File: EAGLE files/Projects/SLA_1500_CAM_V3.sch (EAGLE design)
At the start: 90 parts, among them J4 MOLEX 53398-0471, J5 MOLEX 53398-04, U11 TXS0102, U8 TXS0102, U9 TXS0102

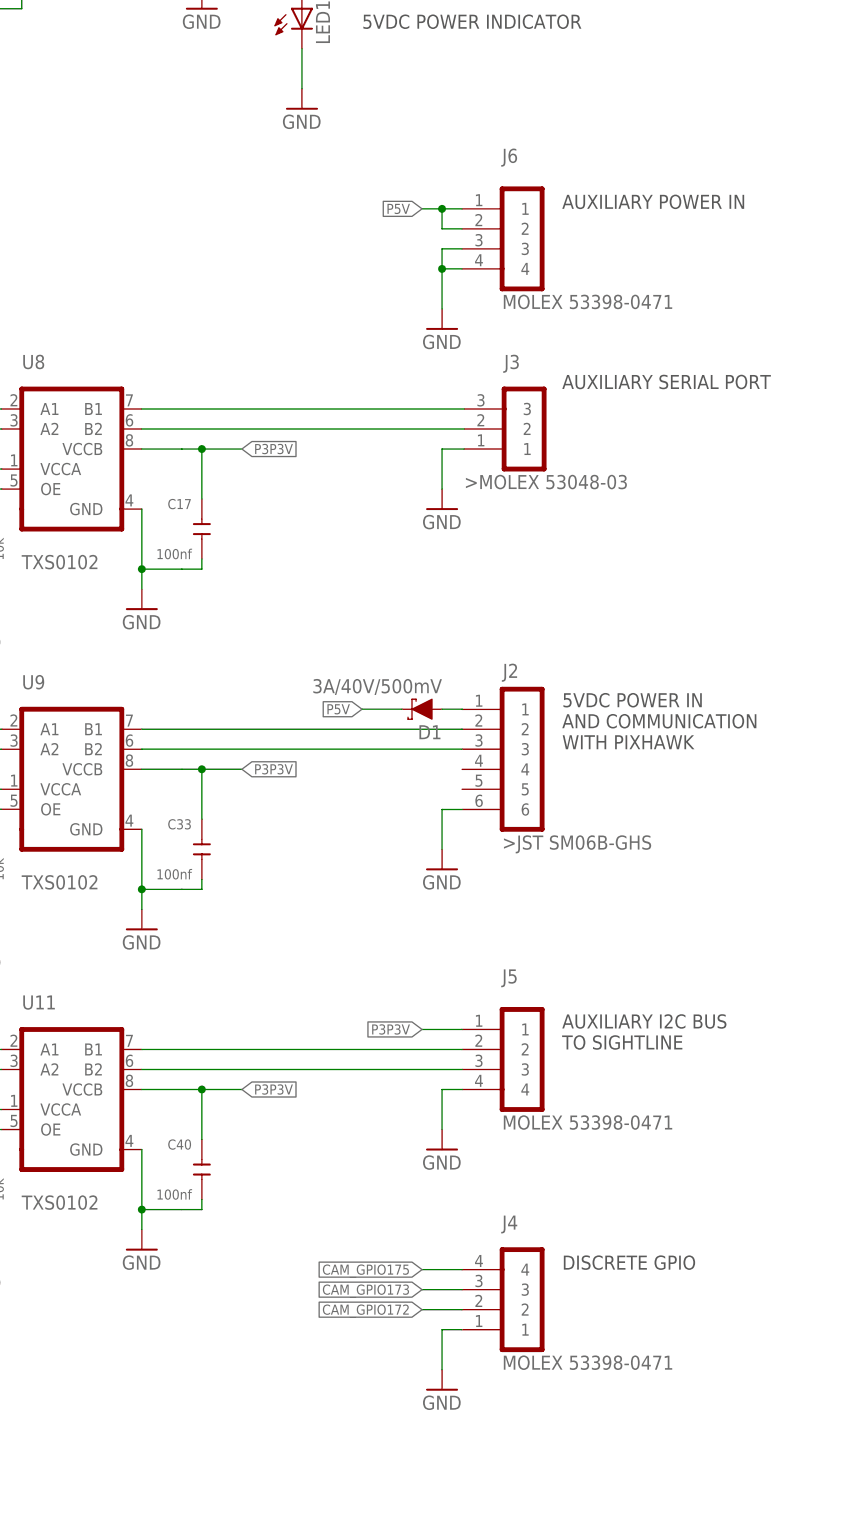
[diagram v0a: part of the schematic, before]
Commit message: Update SLA1500_CAM REV 3.0
Replaced vertical Molex connectors with right angle Molex connectors
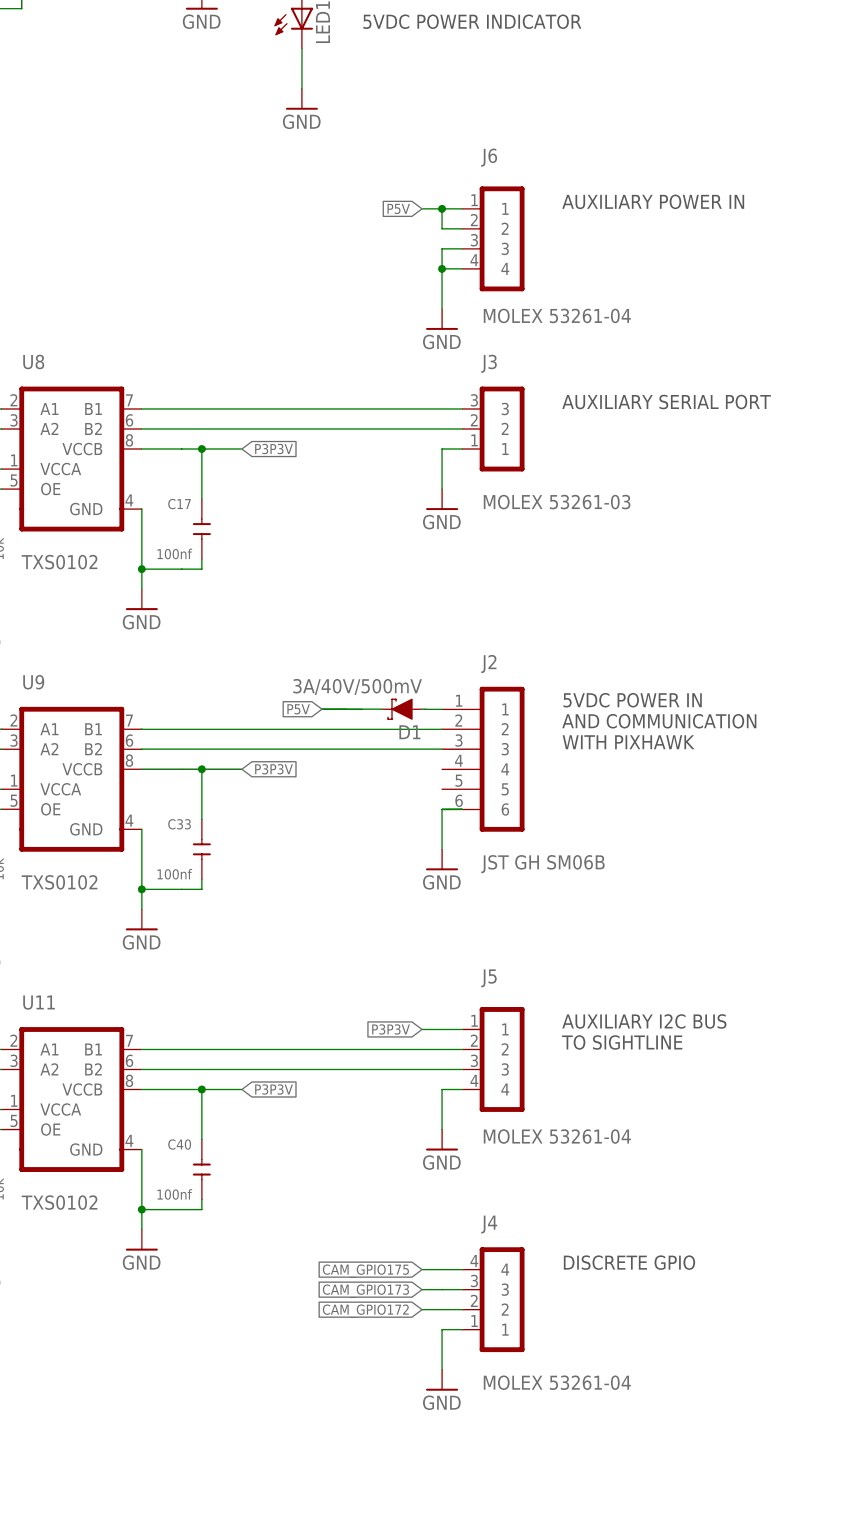
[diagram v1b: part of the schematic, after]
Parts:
- J2: value (none) -> JST GH SM06B
- J3: value (none) -> MOLEX 53261-03; device Sightline:MOLEX_53048-03 -> Sightline:MOLEX53261-03
- J4: value MOLEX 53398-0471 -> MOLEX 53261-04; device Sightline:MOLEX_53398-04 -> Sightline:MOLEX53261-04
- J5: value MOLEX 53398-04 -> MOLEX 53261-04; device Sightline:MOLEX_53398-04 -> Sightline:MOLEX53261-04
- J6: value (none) -> MOLEX 53261-04; device Sightline:MOLEX_53398-04 -> Sightline:MOLEX53261-04
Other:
- note removed: "MOLEX 53398-0471"
- moved on the sheet: D1
